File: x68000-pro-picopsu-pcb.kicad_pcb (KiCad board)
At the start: 2 copper layers, 209 x 98 mm, 22 parts, among them J1 Fan Header, J2 Screw_Terminal_01x07, J3 Screw_Terminal_01x07, J4 PicoPSU, U1 74LS04

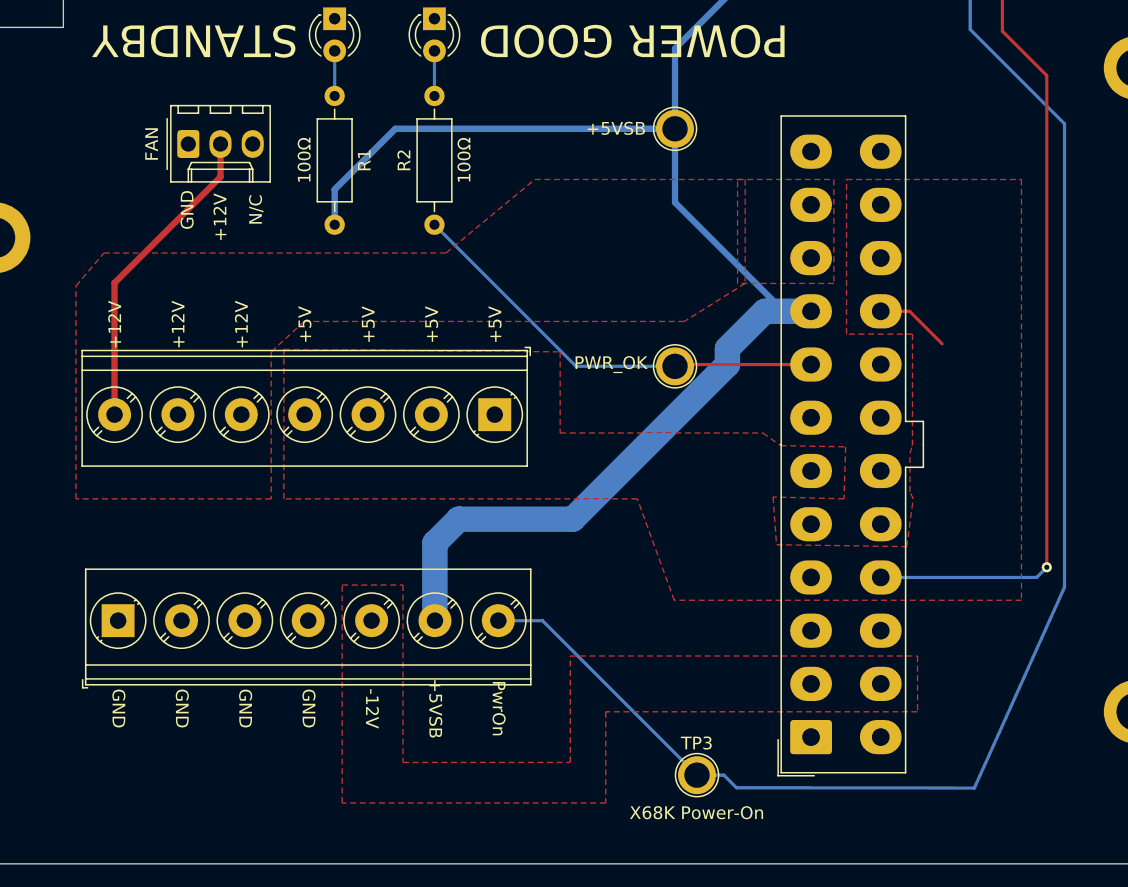
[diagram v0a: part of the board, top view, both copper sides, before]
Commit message: Moved PicoPSU north, no thermal reliefs for ATX
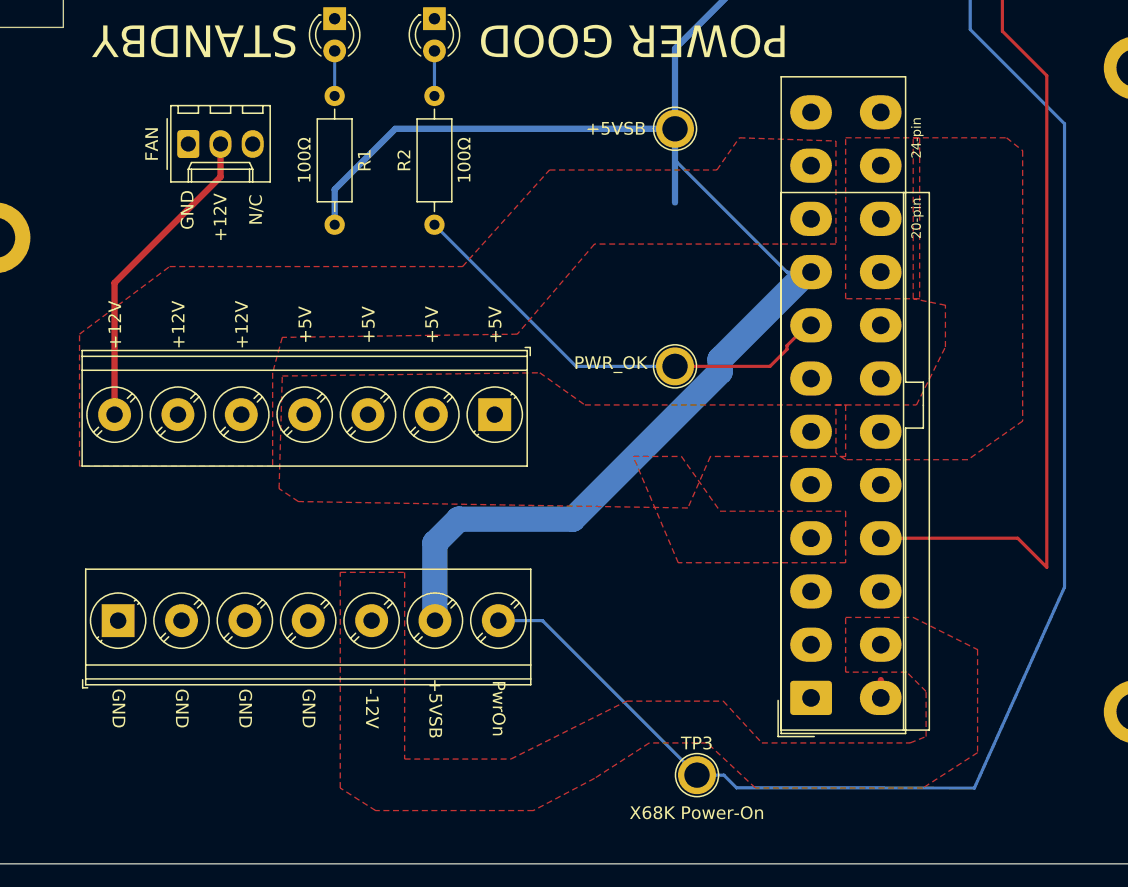
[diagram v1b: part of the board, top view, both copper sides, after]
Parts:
- moved J4 3.09 mm to (91.0, 136.9)
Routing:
- net /PSU_5V: track 5.91 -> 0.00 mm
- net /PSU_5V_STANDBY: track 169.7 -> 173.4 mm
- net /PWR_OK: track 34.6 -> 36.3 mm
- net /~PS_ON: track 84.7 -> 85.3 mm, vias 1 -> 0
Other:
- board text added: "20-pin"
- board text added: "24-pin"
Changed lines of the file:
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@@
   (general
     (thickness 1.6)
-    (drawings 45)
-    (tracks 55)
+    (drawings 54)
+    (tracks 57)
     (zones 0)
     (modules 22)
@@
   )
   (module Connector_Molex:Molex_Mini-Fit_Jr_5566-24A_2x12_P4.20mm_Vertical (layer F.Cu)
-    (at 91 140 90)
+    (at 91 136.906 90)
     (descr "Molex Mini-Fit Jr. Power Connectors, old mpn/engineering number: 5566-24A, example for new mpn: 39-28-x24x, 12 Pins per row, Mounting:  (http://www.molex.com/pdm_docs/sd/039281043_sd.pdf), generated with kicad-footprint-generator")
     (tags "connector Molex Mini-Fit_Jr side entry")
@@
     )
   )
+  (gr_line (start 100.33 139.446) (end 100.33 97.028) (layer F.SilkS) (width 0.12))
+  (gr_line (start 98.298 139.446) (end 100.33 139.446) (layer F.SilkS) (width 0.12))
+  (gr_line (start 98.298 97.028) (end 100.33 97.028) (layer F.SilkS) (width 0.12))
+  (gr_text 20-pin (at 99.314 99.06 90) (layer F.SilkS)
+    (effects (font (size 0.75 0.75) (thickness 0.15)))
+  )
+  (gr_text 24-pin (at 99.314 92.71 90) (layer F.SilkS)
+    (effects (font (size 0.75 0.75) (thickness 0.15)))
+  )
+  (gr_line (start 88.646 139.446) (end 88.646 97.028) (layer F.SilkS) (width 0.12))
+  (gr_line (start 98.298 139.446) (end 88.646 139.446) (layer F.SilkS) (width 0.12))
+  (gr_line (start 98.298 97.028) (end 98.298 139.446) (layer F.SilkS) (width 0.12))
+  (gr_line (start 88.646 97.028) (end 98.298 97.028) (layer F.SilkS) (width 0.12))
   (gr_text "special thanks:\nmattsoft for the x68000 og picopsu board" (at 193.548 57.658) (layer B.SilkS)
     (effects (font (size 1 1) (thickness 0.15)) (justify mirror))
@@
   (segment (start 106.097 84.297) (end 109.6 87.8) (width 0.25) (layer F.Cu) (net 6))
   (segment (start 109.6 87.8) (end 109.6 126.6) (width 0.25) (layer F.Cu) (net 6))
-  (segment (start 109.6 126.6) (end 109.6 126.6) (width 0.25) (layer F.Cu) (net 6))
-  (via (at 109.6 126.6) (size 0.8) (drill 0.4) (layers F.Cu B.Cu) (net 6))
-  (segment (start 108.8 127.4) (end 109.6 126.6) (width 0.25) (layer B.Cu) (net 6))
-  (segment (start 96.5 127.4) (end 108.8 127.4) (width 0.25) (layer B.Cu) (net 6))
-  (segment (start 96.5 135.5) (end 96.5 135.8) (width 0.5) (layer F.Cu) (net 7) (status 30))
+  (segment (start 107.306 124.306) (end 96.5 124.306) (width 0.25) (layer F.Cu) (net 6))
+  (segment (start 109.6 126.6) (end 107.306 124.306) (width 0.25) (layer F.Cu) (net 6))
+  (segment (start 96.5 135.5) (end 96.5 135.8) (width 0.5) (layer F.Cu) (net 8) (status 30))
   (segment (start 80.264 97.814) (end 80.264 92) (width 0.5) (layer B.Cu) (net 10) (status 20))
-  (segment (start 88.85 106.4) (end 80.264 97.814) (width 0.5) (layer B.Cu) (net 10))
-  (segment (start 91 106.4) (end 88.85 106.4) (width 0.5) (layer B.Cu) (net 10) (status 10))
   (segment (start 80.264 92) (end 58.2 92) (width 0.5) (layer B.Cu) (net 10) (status 10))
   (segment (start 53.408 96.792) (end 53.408 99.568) (width 0.5) (layer B.Cu) (net 10) (status 20))
@@
   (segment (start 103.557 64.082) (end 105.515 66.04) (width 0.5) (layer B.Cu) (net 10) (status 10))
   (segment (start 103.557 63.682) (end 103.557 64.082) (width 0.5) (layer B.Cu) (net 10) (status 30))
-  (segment (start 87.35 106.4) (end 84.4 109.35) (width 2) (layer B.Cu) (net 10))
-  (segment (start 91 106.4) (end 87.35 106.4) (width 2) (layer B.Cu) (net 10))
-  (segment (start 84.4 110.604002) (end 72.204002 122.8) (width 2) (layer B.Cu) (net 10))
-  (segment (start 84.4 109.35) (end 84.4 110.604002) (width 2) (layer B.Cu) (net 10))
   (segment (start 72.204002 122.8) (end 63.2 122.8) (width 2) (layer B.Cu) (net 10))
   (segment (start 61.322 124.678) (end 61.322 130.81) (width 2) (layer B.Cu) (net 10))
   (segment (start 63.2 122.8) (end 61.322 124.678) (width 2) (layer B.Cu) (net 10))
+  (segment (start 90.7 103.306) (end 83.82 110.186) (width 2) (layer B.Cu) (net 10))
+  (segment (start 91 103.306) (end 90.7 103.306) (width 2) (layer B.Cu) (net 10))
+  (segment (start 83.82 111.184002) (end 72.204002 122.8) (width 2) (layer B.Cu) (net 10))
+  (segment (start 83.82 110.186) (end 83.82 111.184002) (width 2) (layer B.Cu) (net 10))
+  (segment (start 89.1 103.306) (end 80.264 94.47) (width 0.25) (layer B.Cu) (net 10))
+  (segment (start 80.264 94.12132) (end 80.264 92) (width 0.25) (layer B.Cu) (net 10))
+  (segment (start 80.264 94.47) (end 80.264 94.12132) (width 0.25) (layer B.Cu) (net 10))
+  (segment (start 91 103.306) (end 89.1 103.306) (width 0.25) (layer B.Cu) (net 10))
   (segment (start 80.408 110.6) (end 80.264 110.744) (width 0.25) (layer B.Cu) (net 11) (status 30))
   (segment (start 72.458 110.744) (end 61.282 99.568) (width 0.25) (layer B.Cu) (net 11) (status 20))
   (segment (start 80.264 110.744) (end 72.458 110.744) (width 0.25) (layer B.Cu) (net 11) (status 10))
   (segment (start 80.408 110.6) (end 80.264 110.744) (width 0.25) (layer F.Cu) (net 11))
-  (segment (start 91 110.6) (end 80.408 110.6) (width 0.25) (layer F.Cu) (net 11))
-  (segment (start 96.5 106.4) (end 98.78 106.4) (width 0.25) (layer F.Cu) (net 12))
-  (segment (start 98.78 106.4) (end 101.346 108.966) (width 0.25) (layer F.Cu) (net 12))
+  (segment (start 90.7 107.506) (end 91 107.506) (width 0.25) (layer F.Cu) (net 11))
+  (segment (start 89.1 109.106) (end 90.7 107.506) (width 0.25) (layer F.Cu) (net 11))
+  (segment (start 89.1 109.406) (end 89.1 109.106) (width 0.25) (layer F.Cu) (net 11))
+  (segment (start 87.762 110.744) (end 89.1 109.406) (width 0.25) (layer F.Cu) (net 11))
+  (segment (start 80.264 110.744) (end 87.762 110.744) (width 0.25) (layer F.Cu) (net 11))
   (segment (start 69.81 130.81) (end 82 143) (width 0.25) (layer B.Cu) (net 15) (status 20))
   (segment (start 66.322 130.81) (end 69.81 130.81) (width 0.25) (layer B.Cu) (net 15) (status 10))
@@
   )
   (zone (net 7) (net_name /PSU_NEG_12V) (layer F.Cu) (hatch edge 0.508)
-    (connect_pads (clearance 0.508))
+    (connect_pads yes (clearance 0.508))
     (min_thickness 0.254)
     (fill yes (arc_segments 32) (thermal_gap 0.508) (thermal_bridge_width 0.508))
     (polygon
       (pts
-        (xy 58.8 142) (xy 72 142) (xy 72 133.6) (xy 99.4 133.6) (xy 99.4 138)
-        (xy 74.8 138) (xy 74.8 145.2) (xy 54 145.2) (xy 54 128) (xy 58.8 128)
+        (xy 58.928 141.732) (xy 67.31 141.732) (xy 76.454 137.16) (xy 84.074 137.16) (xy 87.122 140.462)
+        (xy 98.806 140.462) (xy 100.076 139.954) (xy 100.076 136.398) (xy 98.552 134.874) (xy 93.726 134.874)
+        (xy 93.726 130.556) (xy 99.06 130.556) (xy 104.14 133.096) (xy 104.14 141.224) (xy 99.822 144.018)
+        (xy 86.614 144.018) (xy 82.804 140.462) (xy 78.232 140.462) (xy 73.914 143.256) (xy 69.088 145.796)
+        (xy 56.642 145.796) (xy 53.848 144.018) (xy 53.848 127) (xy 58.928 127)
       )
     )
   )
   (zone (net 12) (net_name /PSU_5V) (layer F.Cu) (hatch edge 0.508)
-    (connect_pads (clearance 0.508))
+    (connect_pads yes (clearance 0.508))
     (min_thickness 0.254)
     (fill yes (arc_segments 32) (thermal_gap 0.508) (thermal_bridge_width 0.508))
     (polygon
       (pts
-        (xy 107.6 129.2) (xy 80.2 129.2) (xy 77.290909 121.2) (xy 49.4 121.2) (xy 49.4 109.4)
-        (xy 71.2 109.6) (xy 71.2 116) (xy 87.2 116) (xy 88.6 117) (xy 93.726 117.094)
-        (xy 93.6 121.2) (xy 87.996 121.052) (xy 88.28 124.82) (xy 98.552 124.968) (xy 99.06 121.2)
-        (xy 98.806 120.65) (xy 98.806 117.602) (xy 99 117) (xy 99 108.2) (xy 93.8 108.2)
-        (xy 93.8 96) (xy 107.6 96)
+        (xy 73.152 113.792) (xy 93.726 113.792) (xy 93.726 117.856) (xy 83.058 117.856) (xy 81.28 121.92)
+        (xy 50.546 121.412) (xy 49.022 120.396) (xy 49.276 111.506) (xy 69.596 111.252)
       )
     )
   )
-  (zone (net 16) (net_name /PSU_12V) (layer F.Cu) (hatch edge 0.508)
-    (connect_pads (clearance 0.508))
+  (zone (net 12) (net_name /PSU_5V) (layer F.Cu) (hatch edge 0.508)
+    (connect_pads yes (clearance 0.508))
     (min_thickness 0.254)
     (fill yes (arc_segments 32) (thermal_gap 0.508) (thermal_bridge_width 0.508))
     (polygon
       (pts
-        (xy 92.8 104.2) (xy 85.2 104.2) (xy 85.2 96) (xy 92.8 96)
+        (xy 83.82 122.174) (xy 93.726 122.174) (xy 93.726 126.238) (xy 80.518 126.238) (xy 76.962 117.856)
+        (xy 80.772 117.856)
       )
     )
   )
-  (zone (net 16) (net_name /PSU_12V) (layer F.Cu) (hatch edge 0.508)
-    (connect_pads (clearance 0.508))
+  (zone (net 12) (net_name /PSU_5V) (layer F.Cu) (hatch edge 0.508)
+    (connect_pads yes (clearance 0.508))
     (min_thickness 0.254)
     (fill yes (arc_segments 32) (thermal_gap 0.508) (thermal_bridge_width 0.508))
     (polygon
       (pts
-        (xy 85.8 104.2) (xy 81 107.2) (xy 51 107.2) (xy 48.4 109.6) (xy 48.4 121.2)
-        (xy 33 121.2) (xy 33 104.4) (xy 35.2 101.8) (xy 62.2 101.8) (xy 69.2 96)
-        (xy 85.8 96)
+        (xy 99.568 105.41) (xy 93.726 105.41) (xy 93.726 92.71) (xy 99.568 92.71)
       )
     )
+  )
+  (zone (net 16) (net_name /PSU_12V) (layer F.Cu) (hatch edge 0.508)
+    (connect_pads yes (clearance 0.508))
+    (min_thickness 0.254)
+    (fill yes (arc_segments 32) (thermal_gap 0.508) (thermal_bridge_width 0.508))
+    (polygon
+      (pts
+        (xy 92.964 101.092) (xy 73.914 101.092) (xy 67.818 108.204) (xy 49.276 108.458) (xy 48.514 111.252)
+        (xy 48.514 118.618) (xy 33.274 118.618) (xy 33.274 108.204) (xy 40.386 102.87) (xy 63.5 102.87)
+        (xy 70.358 95.25) (xy 83.566 95.25) (xy 85.344 92.71) (xy 92.964 92.964)
+      )
+    )
+  )
+  (zone (net 12) (net_name /PSU_5V) (layer F.Cu) (hatch edge 0.508)
+    (connect_pads yes (clearance 0.508))
+    (min_thickness 0.254)
+    (fill yes (arc_segments 32) (thermal_gap 0.508) (thermal_bridge_width 0.508))
+    (polygon
+      (pts
+        (xy 107.696 93.726) (xy 107.696 115.062) (xy 103.378 118.11) (xy 93.726 118.11) (xy 92.964 117.602)
+        (xy 92.964 113.792) (xy 99.314 113.792) (xy 101.6 109.22) (xy 101.6 105.918) (xy 99.06 105.41)
+        (xy 99.06 92.71) (xy 106.426 92.71)
+      )
+    )

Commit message: Tie unused 74ls04 inputs to ground
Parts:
- added JP1: N/C, Jumper:SolderJumper-2_P1.3mm_Bridged_RoundedPad1.0x1.5mm, B.Cu at (108.7, 75.6)
- added JP2: N/C, Jumper:SolderJumper-2_P1.3mm_Bridged_RoundedPad1.0x1.5mm, B.Cu at (113.8, 75.6)
- added JP3: N/C, Jumper:SolderJumper-2_P1.3mm_Bridged_RoundedPad1.0x1.5mm, B.Cu at (116.3, 59.4)
- added JP4: N/C, Jumper:SolderJumper-2_P1.3mm_Bridged_RoundedPad1.0x1.5mm, B.Cu at (111.0, 59.6)
- added JP5: N/C, Jumper:SolderJumper-2_P1.3mm_Bridged_RoundedPad1.0x1.5mm, B.Cu at (106.2, 59.7)
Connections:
- U1 pad 10: (no net) -> Net-(U1-Pad10)
- U1 pad 11: (no net) -> Net-(JP4-Pad2)
- U1 pad 12: (no net) -> Net-(U1-Pad12)
- U1 pad 13: (no net) -> Net-(JP5-Pad2)
- U1 pad 3: (no net) -> Net-(JP1-Pad2)
- U1 pad 4: (no net) -> Net-(U1-Pad4)
- U1 pad 5: (no net) -> Net-(JP2-Pad2)
- U1 pad 6: (no net) -> Net-(U1-Pad6)
- U1 pad 8: (no net) -> Net-(U1-Pad8)
- U1 pad 9: (no net) -> Net-(JP3-Pad2)
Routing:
- net /PSU_COM: track 0.00 -> 38.7 mm
- net Net-(JP2-Pad2): track 0.00 -> 3.66 mm
- net Net-(JP1-Pad2): track 0.00 -> 3.66 mm
- net Net-(JP3-Pad2): track 0.00 -> 3.63 mm
- net Net-(JP4-Pad2): track 0.00 -> 3.53 mm
- net Net-(JP5-Pad2): track 0.00 -> 3.37 mm
